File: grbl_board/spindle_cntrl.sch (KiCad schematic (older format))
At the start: 58 parts, among them J14 24V_VFD, J15 Spindle, J16 freq, Q1 BSS127S, Q2 BSS127S, Q3 ZVN4306GTA, Q4 IRF9Z24SPBF, U18 6N137, U19 6N137, U20 6N137, U21 BD9G341EFJ, U22 LMV358, U23 OPA2192, U24 L7805

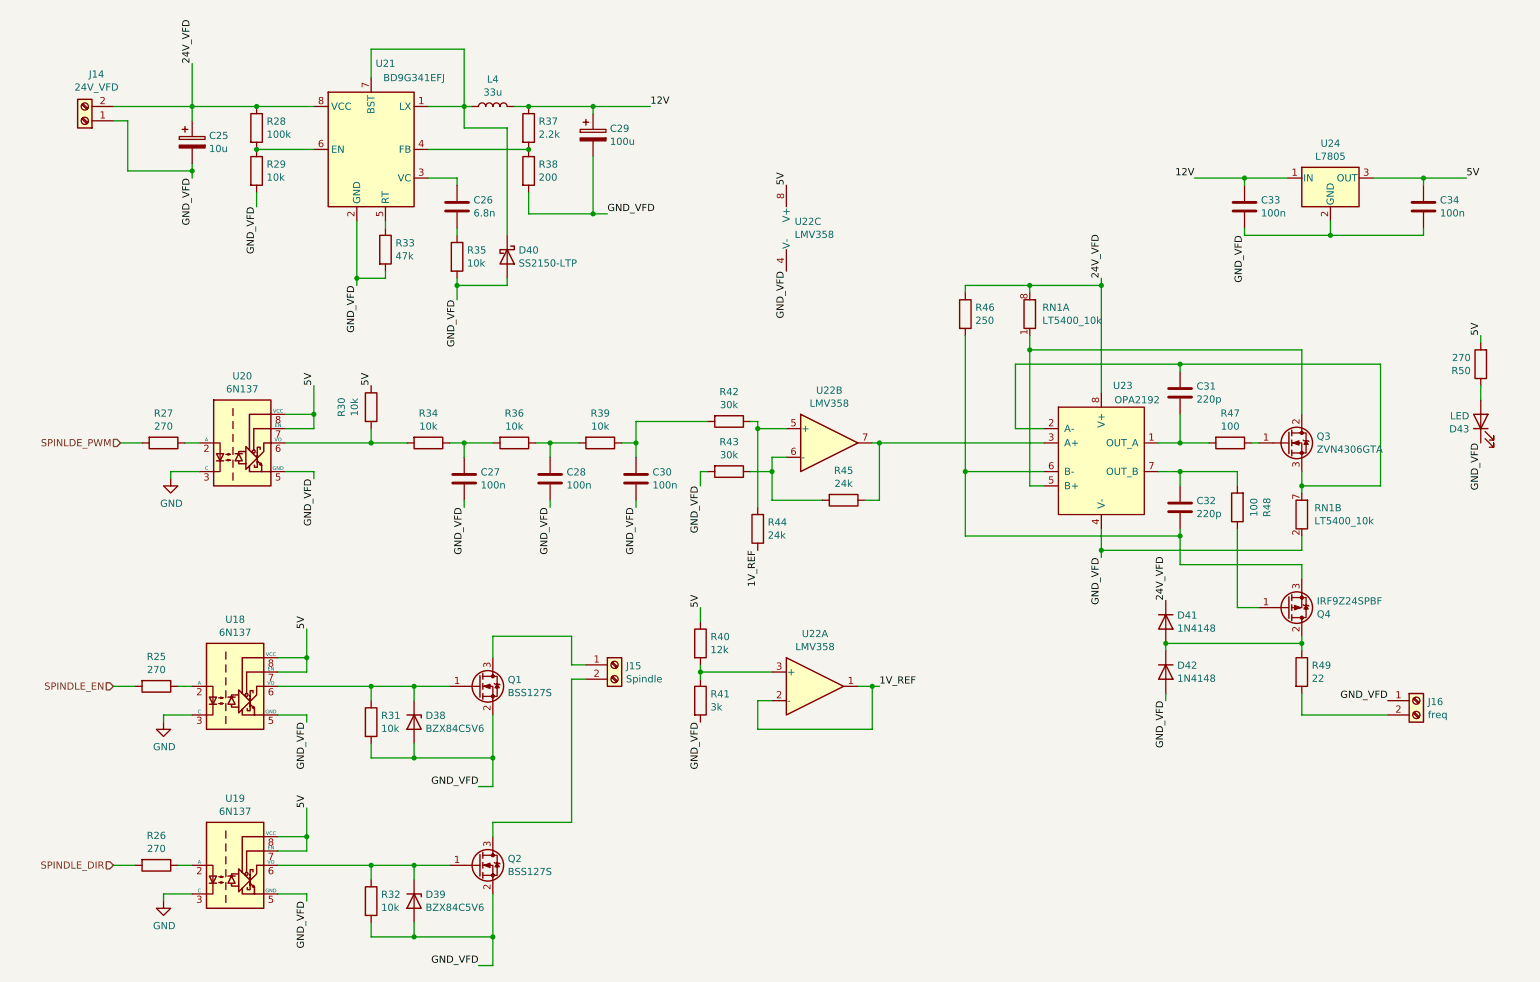
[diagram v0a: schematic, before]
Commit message: fixed pullup resistors on board, and 5v regulator overheating, and stepper driver flipped
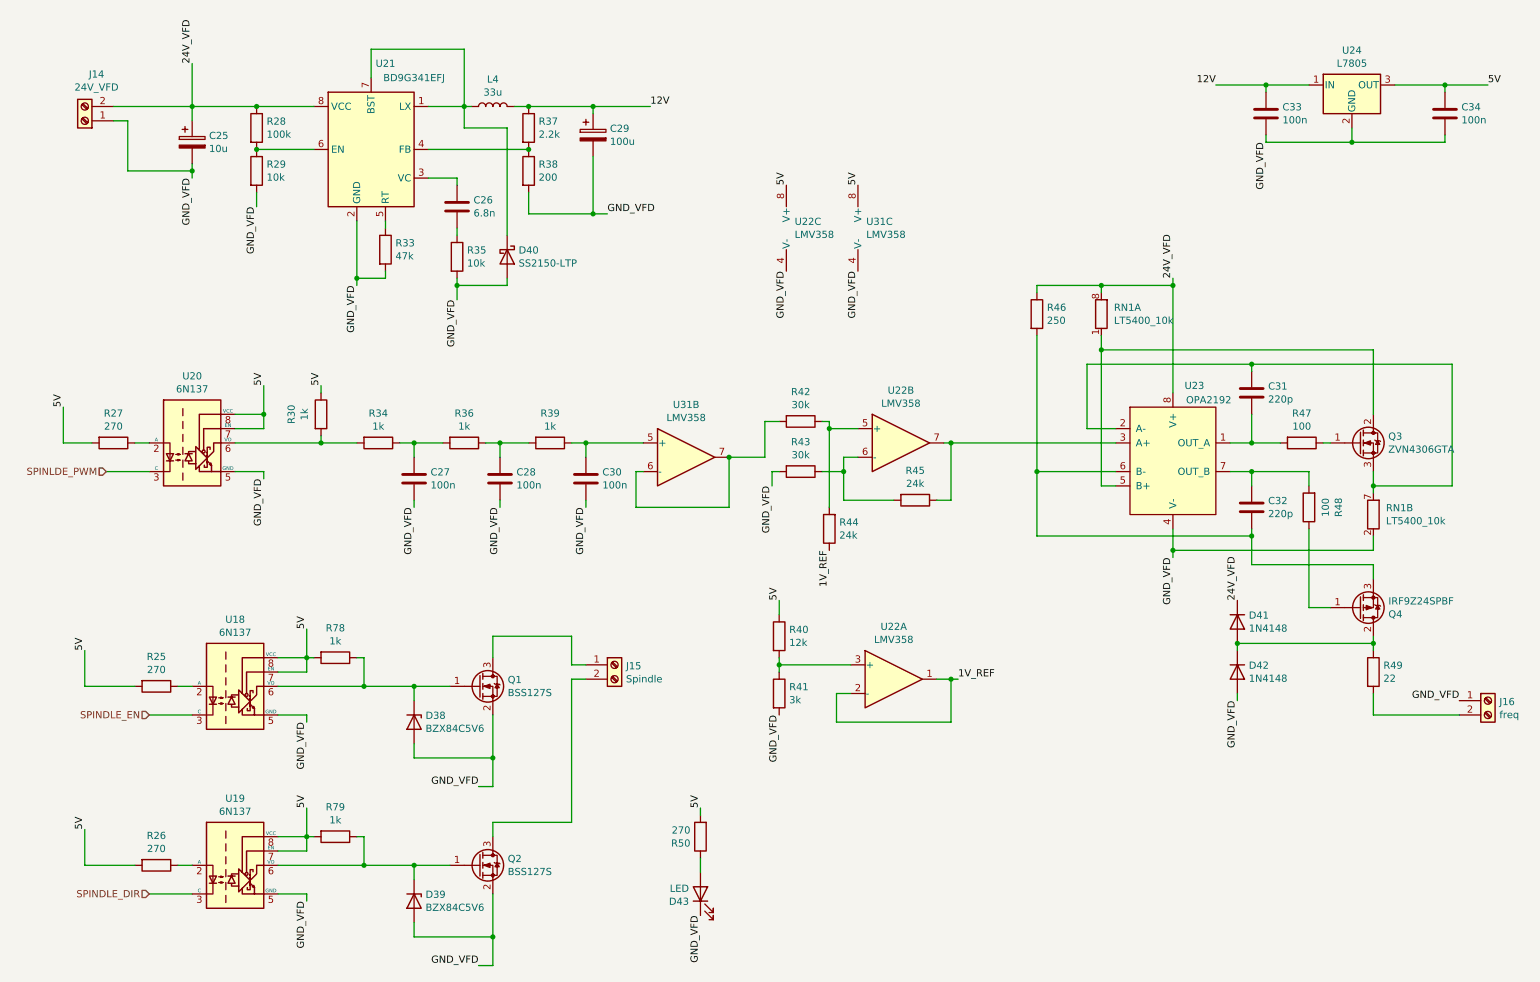
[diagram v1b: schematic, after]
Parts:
- removed R31, R32: 10k, Resistor_SMD:R_0805_2012Metric_Pad1.15x1.40mm_HandSolder, symbol Device:R
- added R78, R79: 1k, Resistor_SMD:R_0805_2012Metric_Pad1.15x1.40mm_HandSolder, symbol Device:R
- added U31: LMV358, Package_SO:SOIC-8_3.9x4.9mm_P1.27mm, symbol Amplifier_Operational:LMV358
- R30, R34, R36, R39: value 10k -> 1k
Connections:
- net 5V: now also R25.2, R26.2, R27.2, R78.2, R79.2, U31.8 (V+)
- net GND_VFD: now also U31.4 (V-)
- net SPINDLE_DIR: now also U19.3 (C); no longer R26.2
- net SPINDLE_EN: now also U18.3 (C); no longer R25.2
- net SPINLDE_PWM: now also U20.3 (C); no longer R27.2
- net at C30.1, R39.1: now also U31.5 (+); no longer R42.2
- net at D38.1 (K), Q1.1 (G), U18.6 (VO): now also R78.1
- net at D39.1 (K), Q2.1 (G), U19.6 (VO): now also R79.1
- removed net GND: U18.3 (C), U19.3 (C), U20.3 (C)
- new net: R42.2, U31.6 (-), U31.7
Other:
- moved on the sheet: C27, C28, C30, C31, C32, C33, C34, D41, D42, D43, J16, Q3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

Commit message: updated board with 24V reg
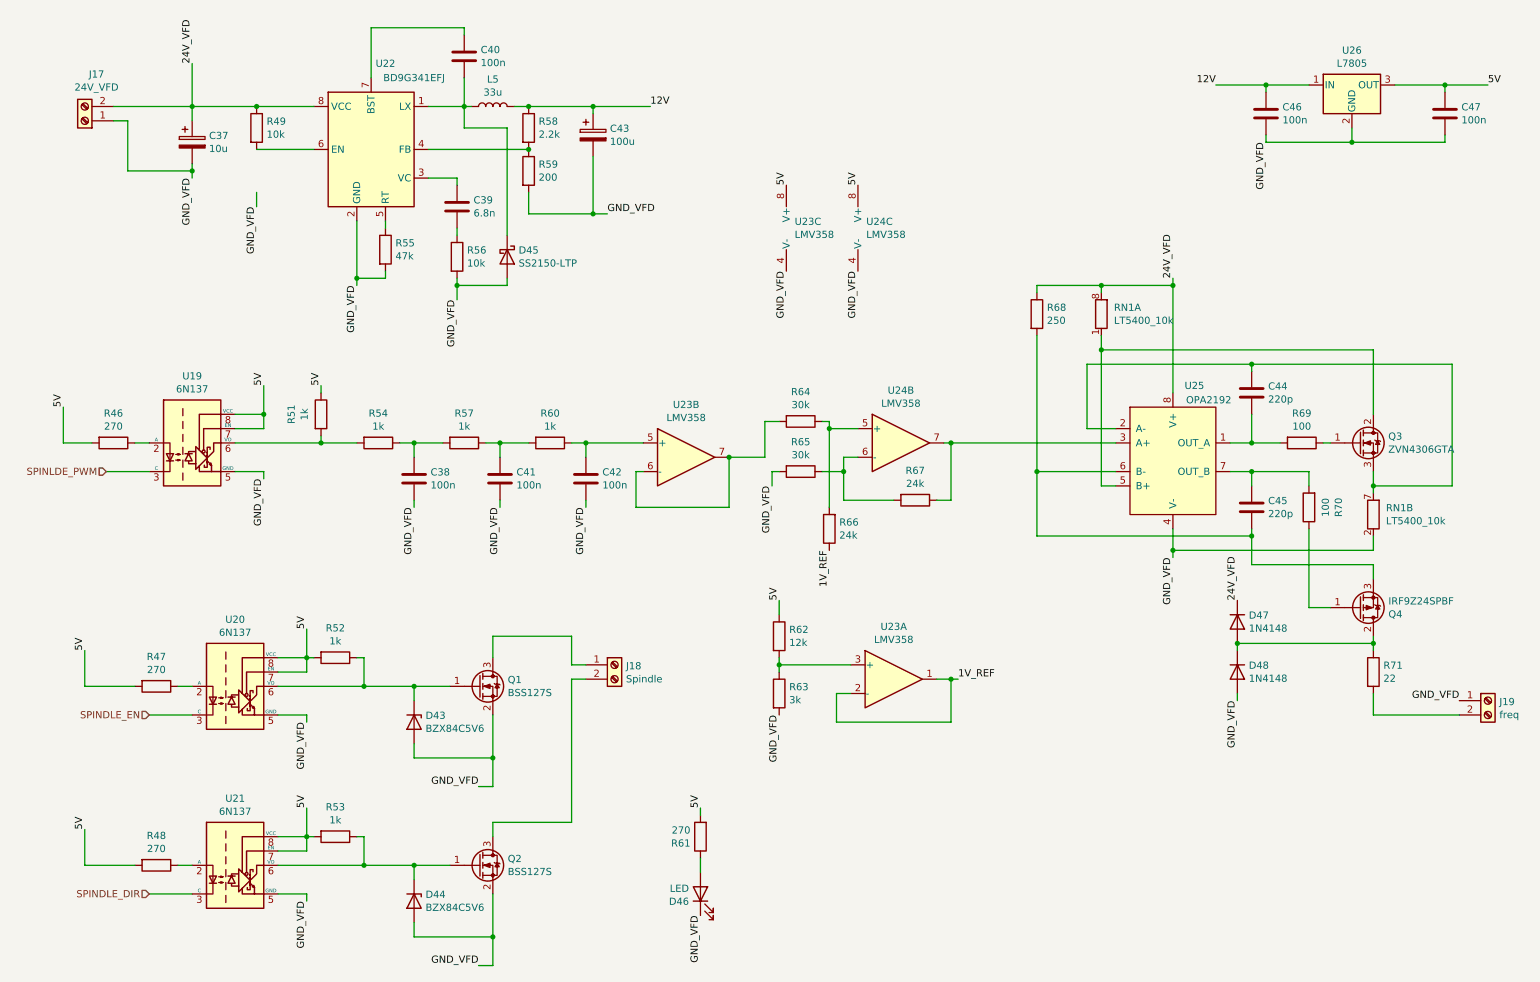
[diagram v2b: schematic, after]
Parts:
- removed R28: 100k, Resistor_SMD:R_0603_1608Metric_Pad0.98x0.95mm_HandSolder, symbol Device:R
- removed R29: 10k, Resistor_SMD:R_0805_2012Metric_Pad1.15x1.40mm_HandSolder, symbol Device:R
- added C40: 100n, Capacitor_SMD:C_0603_1608Metric_Pad1.05x0.95mm_HandSolder, symbol Device:C
- added R49: 10k, Resistor_SMD:R_0805_2012Metric_Pad1.15x1.40mm_HandSolder, symbol Device:R
- renumbered C25 to C37, C27 to C38, C26 to C39, C28 to C41, C30 to C42, C29 to C43, C31 to C44, C32 to C45, C33 to C46, C34 to C47, D38 to D43, D39 to D44, D40 to D45, D43 to D46, D41 to D47, D42 to D48, J14 to J17, J15 to J18, J16 to J19, L4 to L5, R27 to R46, R25 to R47, R26 to R48, R30 to R51, R78 to R52, R79 to R53, R34 to R54, R33 to R55, R35 to R56, R36 to R57, R37 to R58, R38 to R59, R39 to R60, R50 to R61, R40 to R62, R41 to R63, R42 to R64, R43 to R65, R44 to R66, R45 to R67, R46 to R68, R47 to R69, R48 to R70, R49 to R71, U20 to U19, U18 to U20, U19 to U21, U21 to U22, U31 to U23, U22 to U23, U31 to U24, U22 to U24, U23 to U25, U24 to U26
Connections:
- net 24V_VFD: now also R49.1
- net at D45.1 (K), L5.1, U22.1 (LX): now also C40.2; no longer U22.7 (BST)
- net at U22.6 (EN): now also R49.2
- new net: C40.1, U22.7 (BST)
